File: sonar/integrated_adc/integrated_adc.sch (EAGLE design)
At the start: 33 parts, among them CON1 UAVCAN_MICRO, CON2 UAVCAN_MICRO, U1 AP2112K-3.3TRG1, U2 TEENSY_3.X_PINOUT, Y1 NX5032

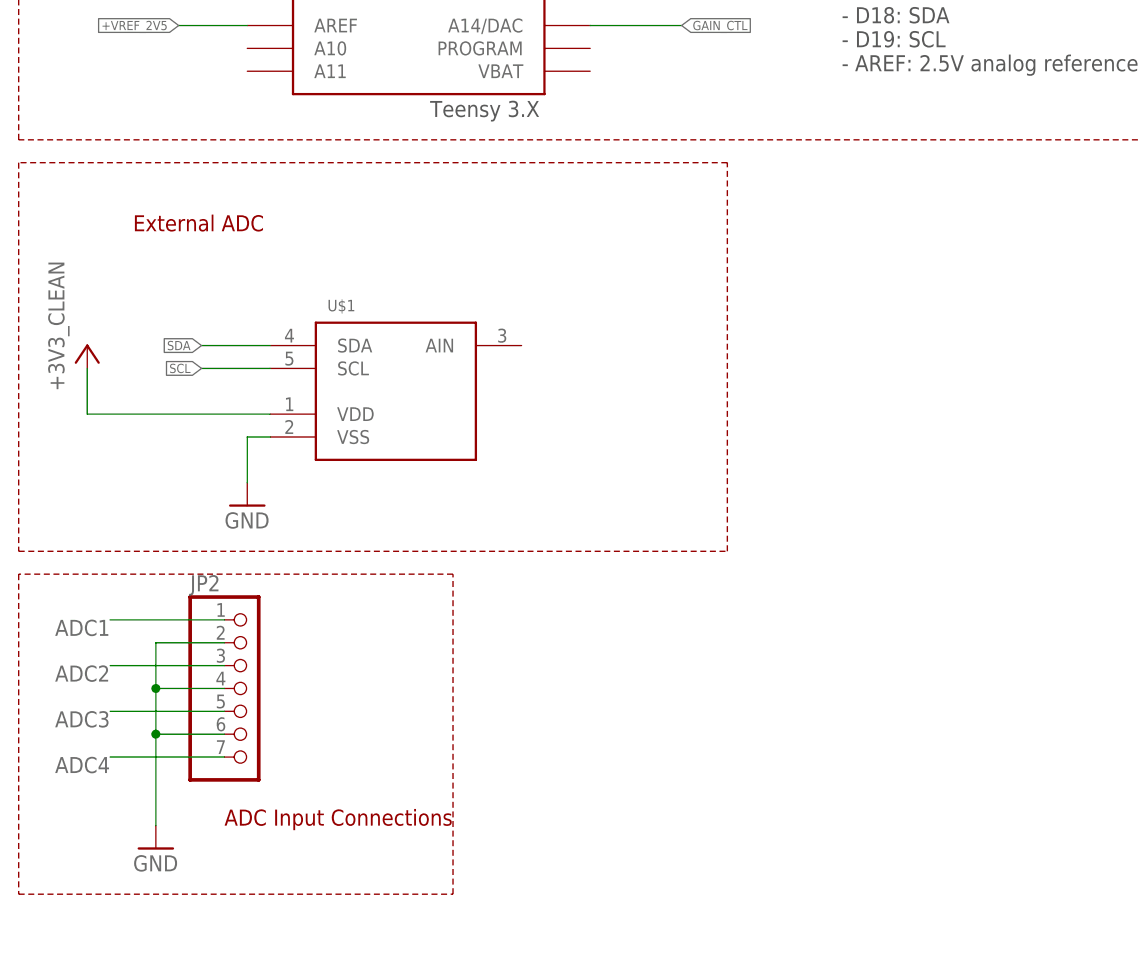
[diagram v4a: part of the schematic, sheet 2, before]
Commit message: Largely finished component placement.
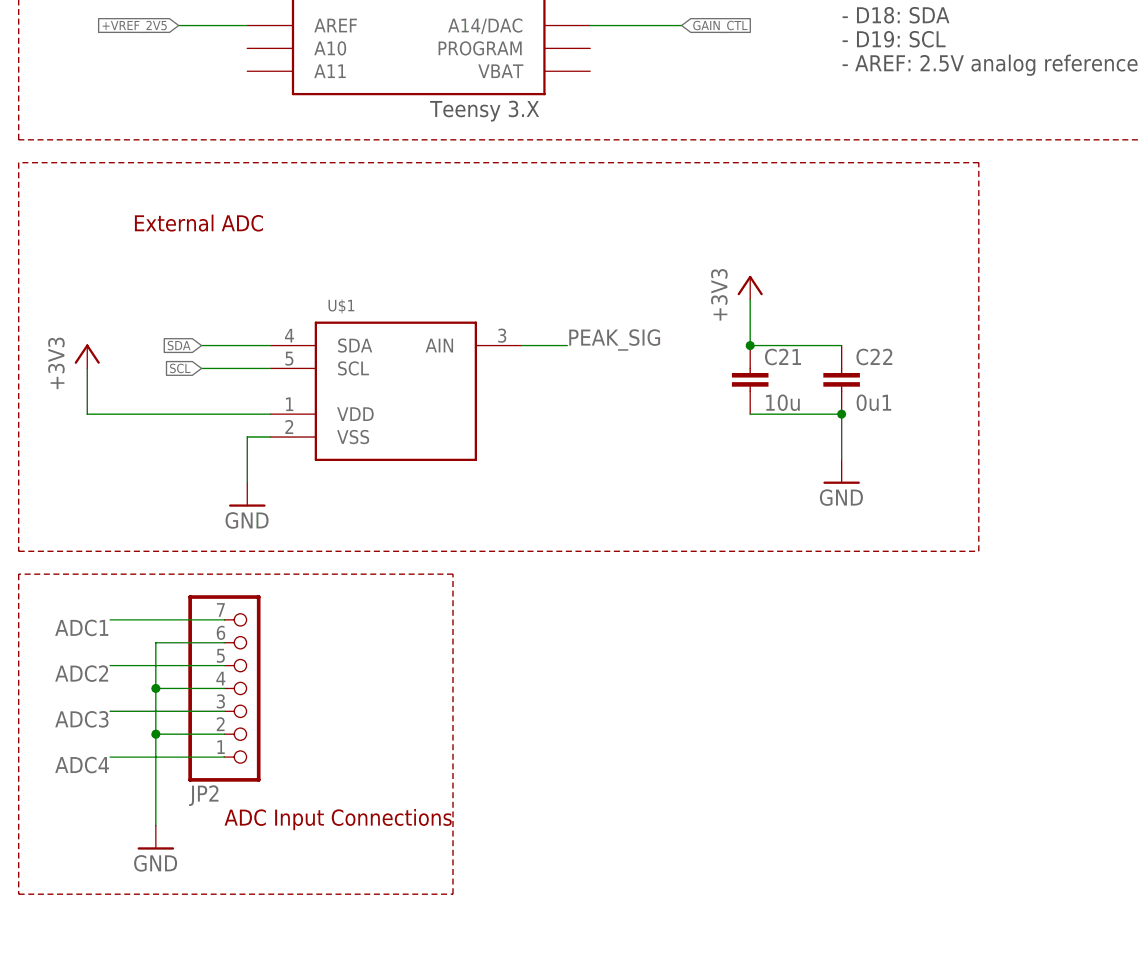
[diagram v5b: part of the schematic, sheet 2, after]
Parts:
- added C19, C20: 1u, resistor:C-EUC0805
- added C21: 10u, resistor:C-EUC0805
- added C22: 0u1, resistor:C-EUC0805
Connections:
- removed net +3V3_CLEAN: U$1.VDD
- net +3V3: now also C20.1, C21.1, C22.1, U$1.VDD
- net ADC1: now also JP2.7; no longer JP2.1
- net ADC2: now also JP2.5; no longer JP2.3
- net ADC3: now also JP2.3; no longer JP2.5
- net ADC4: now also JP2.1; no longer JP2.7
- net GND: now also C19.2, C20.2, C21.2, C22.2, JP3.6; no longer JP3.1
- net N$2: now also JP3.5; no longer JP3.2
- net N$3: now also JP3.4; no longer JP3.3
- net N$9: now also JP3.1; no longer JP3.6
- net PEAK_SIG: now also U$1.AIN
- net UART1_RX: now also JP3.2; no longer JP3.5
- net UART1_TX: now also JP3.3; no longer JP3.4
- net VCC: now also C19.1
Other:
- moved on the sheet: JP2, JP3

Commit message: Theoretically finished integrated ADC system.
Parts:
- added R4, R5: 10k, resistor:R-EU_R0805
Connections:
- net USB_DM renamed USB_D_N
- net USB_DP renamed USB_D_P
- removed net +5V: U$2.VDD
- removed net N$6: CON1.GND, CON1.TABS, CON2.GND, CON2.TABS
- removed net N$7: U$3G$6.VSS
- removed net SWDCLK: U$3G$1.PA14
- net +3V3: now also R4.2, R5.2
- net GAIN_CTL: now also U$3G$4.PD5
- net GND: now also CON1.GND, CON1.TABS, CON2.GND, CON2.TABS, U$3G$6.VSS
- net GPIO_0: now also U$3G$4.PD0
- net GPIO_1: now also U$3G$4.PD1
- net GPIO_2: now also U$3G$4.PD2
- net GPIO_3: now also U$3G$4.PD3
- net GPIO_4: now also U$3G$4.PD4
- net SCL: now also R4.1
- net SDA: now also R5.1
- net SWCLK: now also U$3G$1.PA14
- net VCC: now also U$2.VDD
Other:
- note added: "4-Layer PCB from JLCPCB. Stackup: JLC7628"
- note added: "From JLCPCB calculator, for 90ohm differential pair: 8 mil spacing, 10 mil trace width."

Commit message: I should really be studying for finals.
Final tweaks to schematic.
I can't find anything terrible about either the layout or the schematic,
but I'm certain there's something wrong.
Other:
- note added: "I2C Pullups"
- moved on the sheet: R2, R3, R4, R5

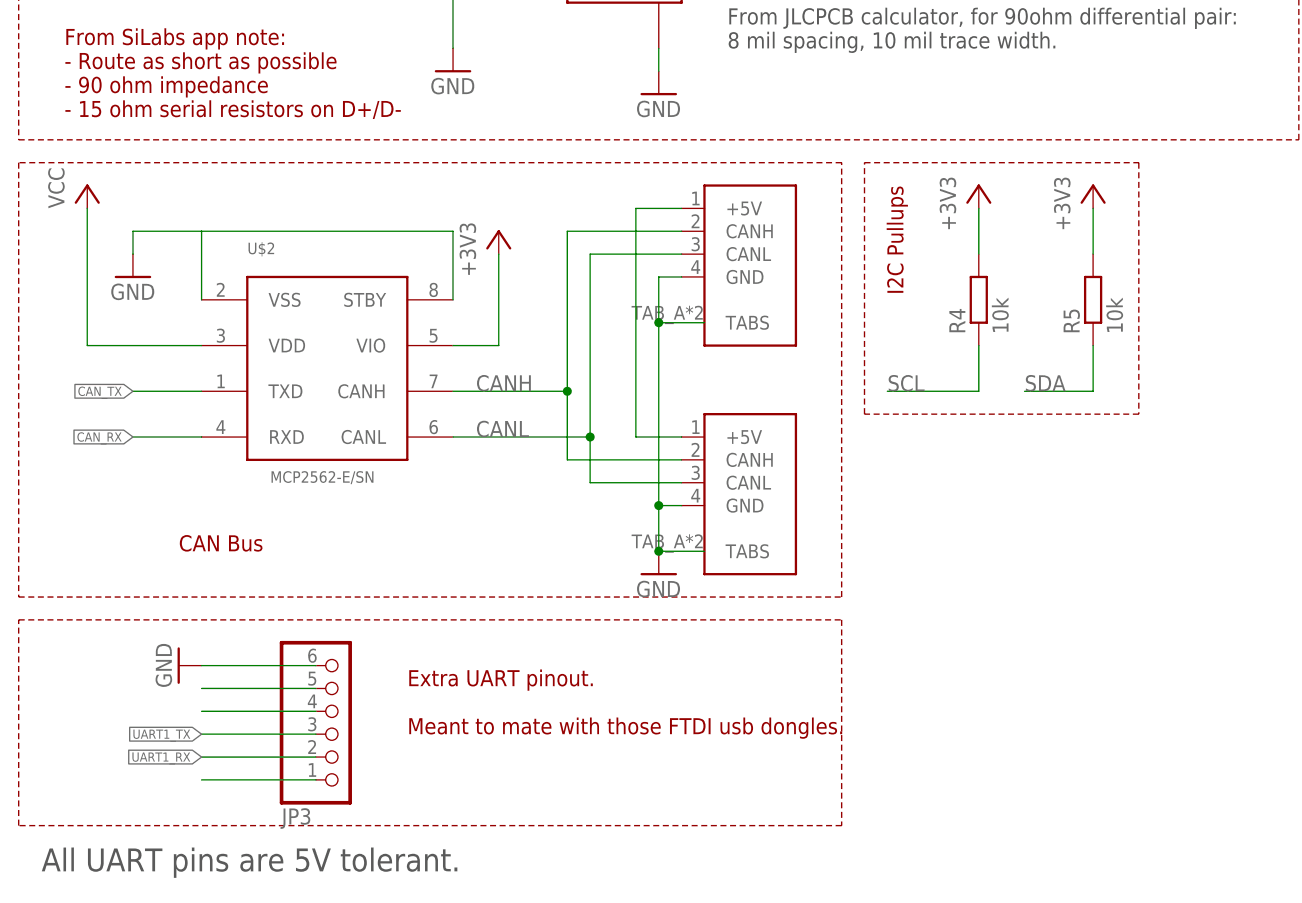
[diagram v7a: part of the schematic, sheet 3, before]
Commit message: Finished BOM, added silkscreen info.
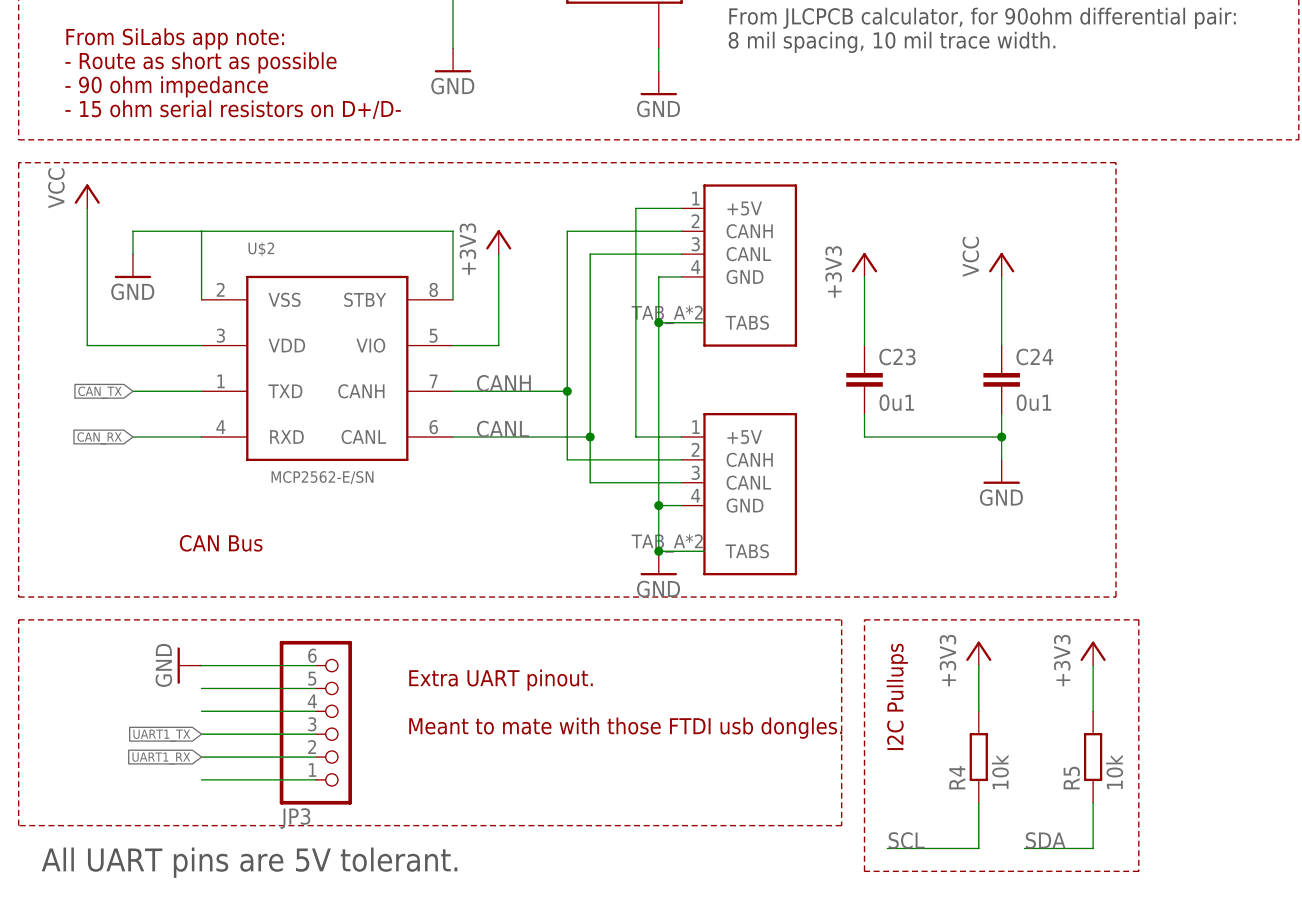
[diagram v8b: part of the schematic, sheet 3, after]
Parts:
- added ARVP1: ARVP_LOGO, ARVP:ARVP_LOGO
- added C23, C24: 0u1, resistor:C-EUC0805
- C1, C2: value 22pF -> 8pF
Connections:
- net +3V3: now also C23.1
- net GND: now also C23.2, C24.2
- net VCC: now also C24.1
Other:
- note added: "Load Capacitance calculated using ST AN2867. Using Cs = 4pF, and Cl = 8pF."
- note removed: "22pF loading capacitors not verified for 12MHz!"
- moved on the sheet: R4, R5
